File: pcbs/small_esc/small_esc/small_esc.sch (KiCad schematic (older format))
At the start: 48 parts, among them J1 Conn_01x04_Female, J2 Conn_01x13_Female, J3 Conn_01x10_Female, J4 Conn_01x03_Female, SW1 load iar, SW10 1, SW11 2, SW12 3, SW13 4, SW14 5, SW15 6, SW16 7, SW17 8, SW18 9, SW19 0, SW2 load addr, SW20 A, SW21 B, SW22 C, SW23 ki reset, SW24 run, SW25 stop, SW26 dump, SW27 check, SW28 reload, SW3 load store, SW4 decr addr, SW5 incr addr, SW6 normal reset, SW7 clear, SW8 minus, SW9 point, U1 Pico, U2 AP1117-33

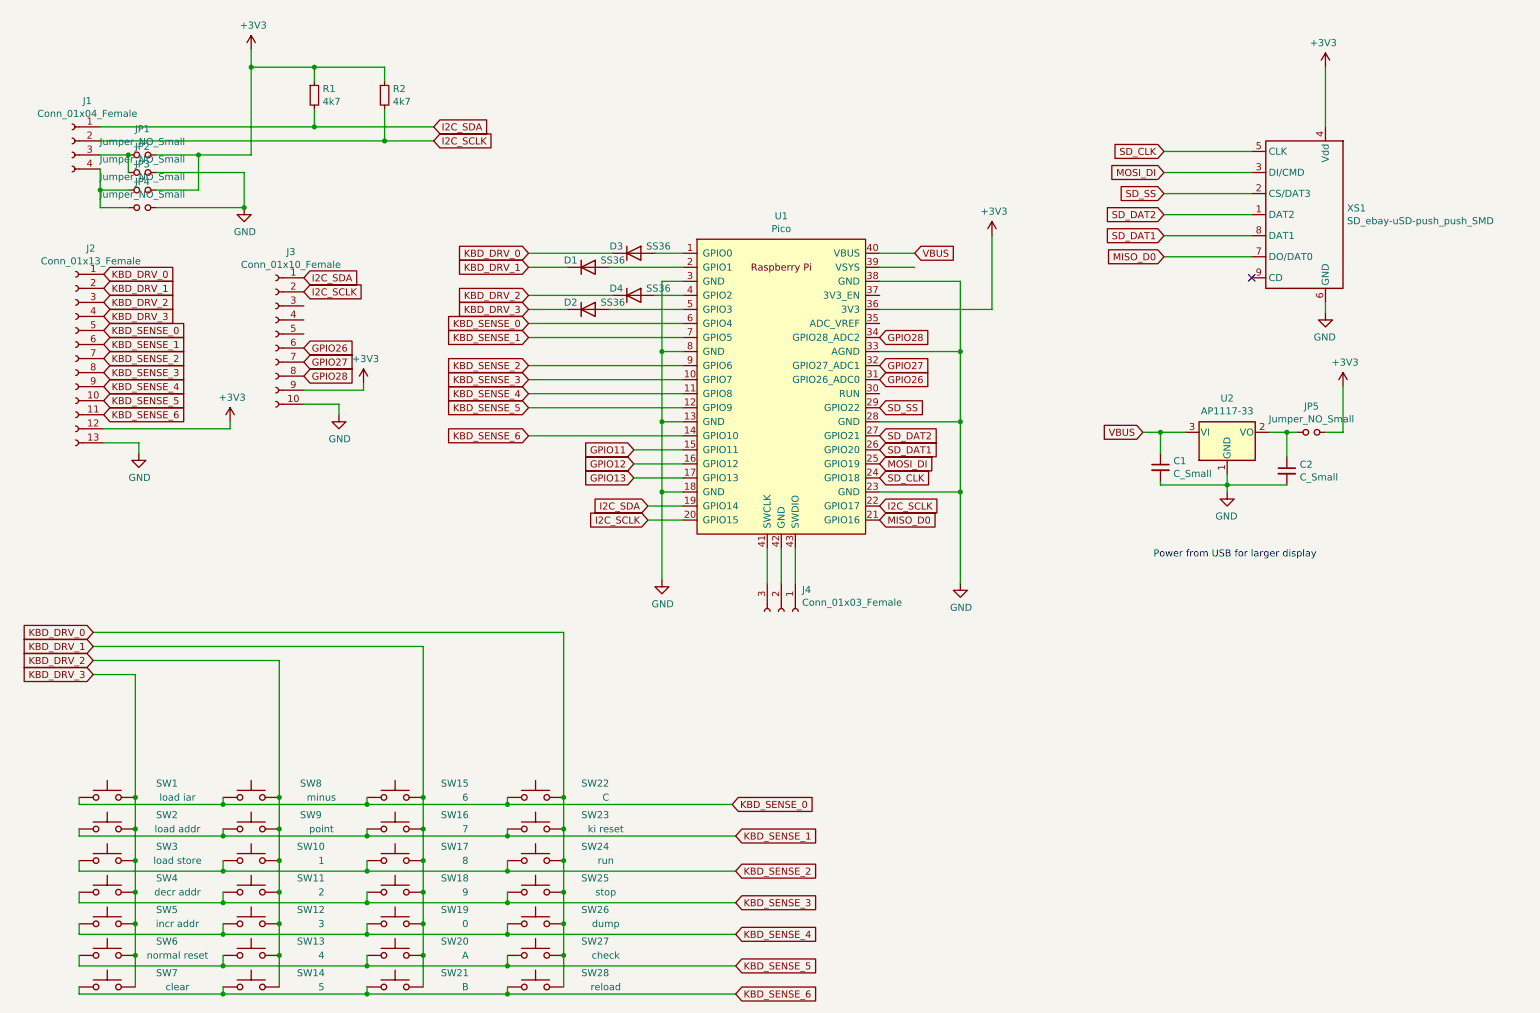
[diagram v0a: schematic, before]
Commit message: Added PCB artwork for V1.0 small PCb version. Pico, small keyboard and a 0.96" OLED screen. Options for mounting screen and powering the board. GPIOs run to connectors so external keyboard and display an option. SD card slot for code storage/cassette emulation.
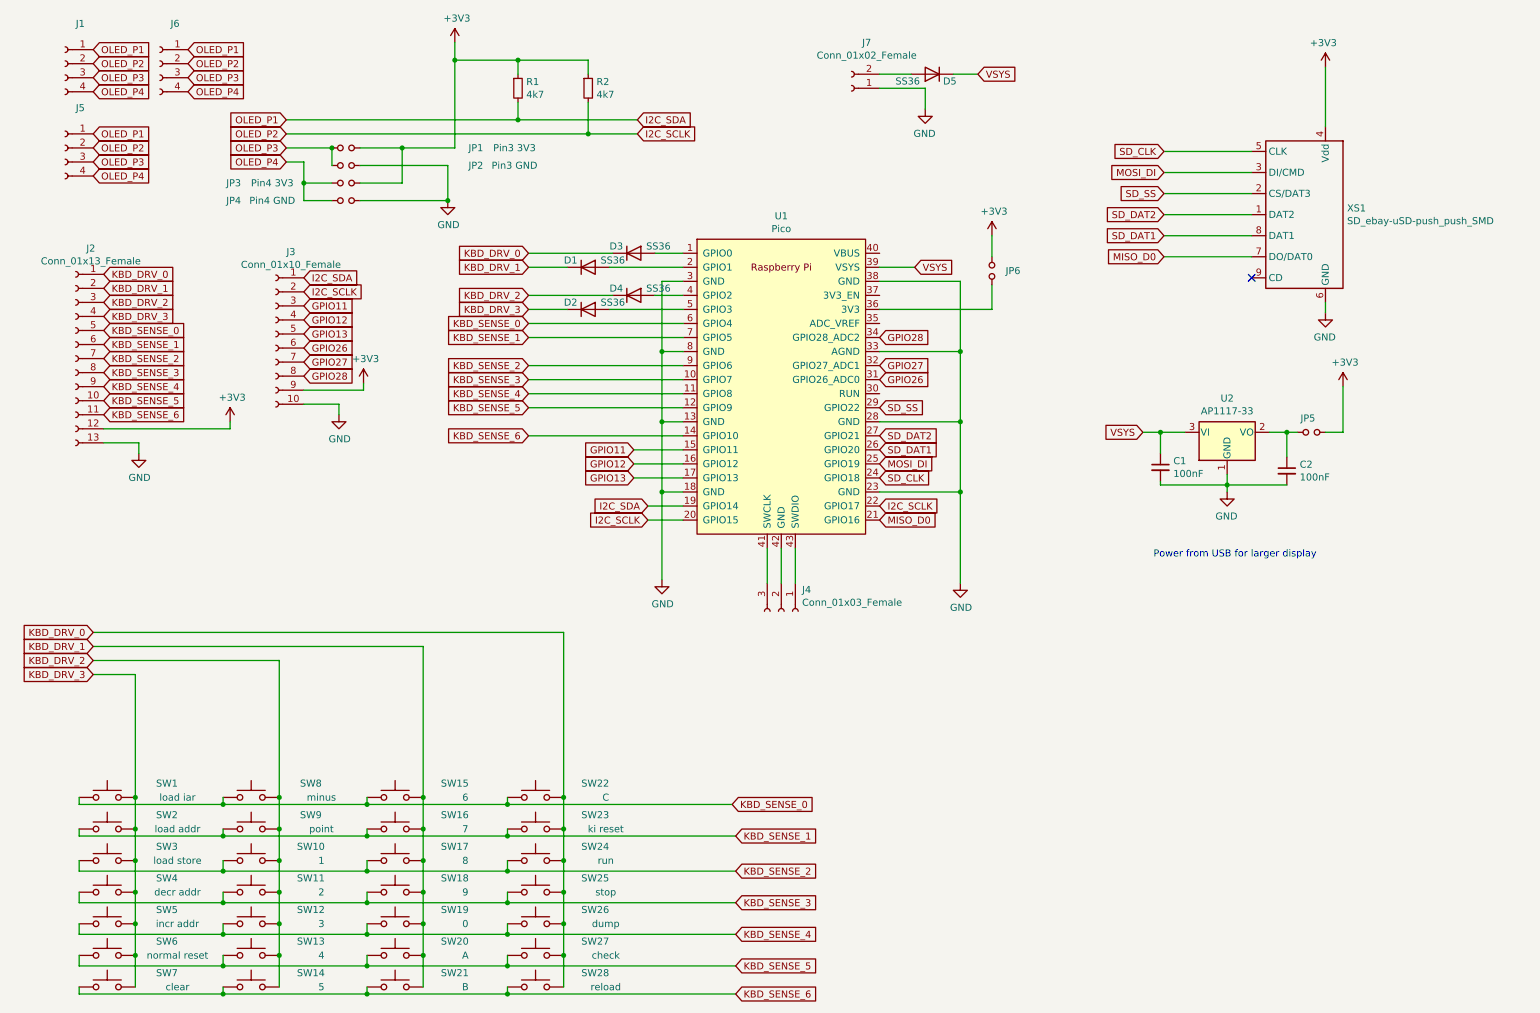
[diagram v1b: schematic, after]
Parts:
- added D5: SS36, Diode_SMD:D_SOD-123, symbol Device:D
- added J5, J6: Conn_01x04_Female, Connector_PinHeader_2.54mm:PinHeader_1x04_P2.54mm_Vertical, symbol Connector:Conn_01x04_Female
- added J7: Conn_01x02_Female, Connector_PinSocket_2.54mm:PinSocket_1x02_P2.54mm_Vertical, symbol Connector:Conn_01x02_Female
- added JP6: Jumper_NO_Small, Jumper:SolderJumper-2_P1.3mm_Open_TrianglePad1.0x1.5mm, symbol Device:Jumper_NO_Small
- C1, C2: value C_Small -> 100nF
- JP1: value Jumper_NO_Small -> Pin3 3V3
- JP2: value Jumper_NO_Small -> Pin3 GND
- JP3: value Jumper_NO_Small -> Pin4 3V3
- JP4: value Jumper_NO_Small -> Pin4 GND
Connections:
- net +3V3: now also JP6.1; no longer U1.36 (3V3)
- net GND: now also J7.1 (Pin_1)
- net GPIO11: now also J3.3 (Pin_3)
- net GPIO12: now also J3.4 (Pin_4)
- net GPIO13: now also J3.5 (Pin_5)
- net I2C_SCLK: now also J5.2 (Pin_2), J6.2 (Pin_2)
- net I2C_SDA: now also J5.1 (Pin_1), J6.1 (Pin_1)
- net VSYS: now reaches U1.39 (VSYS)
- net VSYS: now also C1.1, U2.3 (VI), D5.1 (K)
- net OLED_P3: now reaches J1.3 (Pin_3), JP1.1, JP2.1
- net OLED_P3: now also J5.3 (Pin_3), J6.3 (Pin_3)
- net OLED_P4: now reaches J1.4 (Pin_4), JP3.1, JP4.1
- net OLED_P4: now also J5.4 (Pin_4), J6.4 (Pin_4)
- removed net VBUS: C1.1, U1.40 (VBUS), U2.3 (VI)
- new net: JP6.2, U1.36 (3V3)
- new net: D5.2 (A), J7.2 (Pin_2)
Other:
- moved on the sheet: JP1, JP2, JP3, JP4, R1, R2

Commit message: Updates
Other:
- note added: "VSYS can be powered here from a 5V supply. For \nsending 5V out of the PCB, either short the diode\n and use this connector or remove the diode\nand connect the connector to VBUS"
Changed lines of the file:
@@
 Text GLabel 2525 2700 2    50   Input ~ 0
 GPIO12
+Text Notes 7775 825  0    39   ~ 0
+VSYS can be powered here from a 5V supply. For \nsending 5V out of the PCB, either short the diode\n and use this connector or remove the diode\nand connect the connector to VBUS
 $EndSCHEMATC
